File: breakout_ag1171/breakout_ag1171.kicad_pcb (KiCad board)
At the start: 2 copper layers, 70 x 60 mm, 28 parts, among them J1 EXT1, J2 EXT2, J3 Barrel_Jack_Switch, J4 6P6C, J5 FTDI, Q1 Q_NPN_BCE, U1 Ag1171

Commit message: Add KiBot and pdf outputs for breakout_ag1171
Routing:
- net /RING: track 67.7 -> 60.4 mm
- net /TIP: track 69.0 -> 67.0 mm
- net +3V3: track 141.7 -> 140.6 mm
- net GND: track 9.75 -> 10.8 mm, vias 5 -> 6
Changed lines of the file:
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@@
 	(footprint "Diode_THT:D_DO-35_SOD27_P12.70mm_Horizontal"
 		(layer "F.Cu")
-		(at 138.03 107.175)
+		(at 138.06 107.175)
 		(descr "Diode, DO-35_SOD27 series, Axial, Horizontal, pin pitch=12.7mm, , length*diameter=4*2mm^2, , http://www.diodes.com/_files/packages/DO-35.pdf")
 		(tags "Diode DO-35_SOD27 series Axial Horizontal pin pitch 12.7mm  length 4mm diameter 2mm")
@@
 	)
 	(segment
-		(start 124.925 89.941)
+		(start 120.37 98.19)
 		(end 124.925 98.19)
 		(width 0.254)
@@
 	(segment
 		(start 113.03 87.73)
-		(end 122.714 87.73)
-		(width 0.254)
-		(layer "F.Cu")
-		(net 3)
-	)
-	(segment
-		(start 120.37 98.19)
-		(end 124.925 98.19)
+		(end 126.79 87.73)
 		(width 0.254)
 		(layer "F.Cu")
@@
 	)
 	(segment
-		(start 122.714 87.73)
-		(end 124.925 89.941)
-		(width 0.254)
-		(layer "F.Cu")
-		(net 3)
-	)
-	(segment
 		(start 127.1475 98.19)
 		(end 120.37 98.19)
@@
 	)
 	(segment
-		(start 118.956 103.53)
-		(end 118.956 107.213)
+		(start 112.43 100.93)
+		(end 112.43 107.63)
 		(width 0.254)
 		(layer "F.Cu")
@@
 	)
 	(segment
-		(start 128.9525 96.5475)
-		(end 129.33 96.17)
-		(width 0.254)
-		(layer "F.Cu")
-		(net 4)
-	)
-	(segment
-		(start 118.956 107.213)
-		(end 120.188 108.445)
-		(width 0.254)
-		(layer "F.Cu")
-		(net 4)
-	)
-	(segment
-		(start 112.43 107.63)
-		(end 112.43 103.452)
+		(start 129.33 96.17)
+		(end 129.33 70.78)
 		(width 0.254)
 		(layer "F.Cu")
@@
 	)
 	(segment
-		(start 126.741 108.445)
-		(end 128.9525 106.2335)
+		(start 117.83 97.17)
+		(end 116.19 97.17)
 		(width 0.254)
 		(layer "F.Cu")
@@
 	)
 	(segment
-		(start 117.83 97.17)
-		(end 116.299 97.17)
+		(start 116.19 97.17)
+		(end 112.43 100.93)
 		(width 0.254)
 		(layer "F.Cu")
@@
 	)
 	(segment
-		(start 115.654 100.228)
-		(end 118.956 103.53)
+		(start 124.985 108.445)
+		(end 126.741 108.445)
 		(width 0.254)
 		(layer "F.Cu")
@@
 	)
 	(segment
-		(start 115.654 97.815)
-		(end 115.654 100.228)
+		(start 124.17 107.63)
+		(end 124.985 108.445)
 		(width 0.254)
 		(layer "F.Cu")
@@
 	)
 	(segment
-		(start 116.299 97.17)
-		(end 115.654 97.815)
+		(start 126.741 108.445)
+		(end 128.9525 106.2335)
 		(width 0.254)
 		(layer "F.Cu")
@@
 	)
 	(segment
-		(start 120.188 108.445)
-		(end 126.741 108.445)
+		(start 128.9525 96.5475)
+		(end 129.33 96.17)
 		(width 0.254)
 		(layer "F.Cu")
@@
 	)
 	(segment
-		(start 129.33 96.17)
-		(end 129.33 70.78)
+		(start 112.43 107.63)
+		(end 124.17 107.63)
 		(width 0.254)
 		(layer "F.Cu")
@@
 	)
 	(segment
-		(start 112.43 103.452)
-		(end 115.654 100.228)
+		(start 133.853 108.445)
+		(end 135.123 107.175)
 		(width 0.254)
 		(layer "F.Cu")
-		(net 4)
+		(net 5)
 	)
 	(segment
-		(start 137.992 107.213)
+		(start 135.123 107.175)
 		(end 138.03 107.175)
 		(width 0.254)
@@
 	)
 	(segment
-		(start 135.085 107.213)
-		(end 137.992 107.213)
-		(width 0.254)
-		(layer "F.Cu")
-		(net 5)
-	)
-	(segment
-		(start 133.853 108.445)
-		(end 135.085 107.213)
-		(width 0.254)
-		(layer "F.Cu")
-		(net 5)
-	)
-	(segment
 		(start 111.082 72.034)
 		(end 111.086 72.03)
@@
 	)
 	(segment
-		(start 165.68 71.57)
-		(end 164.89 70.78)
-		(width 0.508)
+		(start 113.04 83.083)
+		(end 113.04 81.905)
+		(width 0.254)
 		(layer "F.Cu")
 		(net 6)
@@
 	(segment
 		(start 165.68 74)
-		(end 165.68 71.57)
+		(end 164.592 74)
 		(width 0.508)
 		(layer "F.Cu")
@@
 	)
 	(segment
-		(start 113.04 83.083)
-		(end 113.04 81.905)
-		(width 0.254)
+		(start 165.68 74)
+		(end 165.68 71.57)
+		(width 0.508)
 		(layer "F.Cu")
 		(net 6)
@@
 	)
 	(segment
+		(start 165.68 71.57)
+		(end 164.89 70.78)
+		(width 0.508)
+		(layer "F.Cu")
+		(net 6)
+	)
+	(segment
 		(start 132.164 105.905)
 		(end 131.135 105.905)
@@
 	)
 	(via
+		(at 164.592 74)
+		(size 1)
+		(drill 0.5)
+		(layers "F.Cu" "B.Cu")
+		(net 6)
+	)
+	(via
 		(at 111.082 68.03)
 		(size 0.6)
@@
 	)
 	(segment
-		(start 167.851 78.003)
-		(end 166.64 76.792)
-		(width 0.508)
-		(layer "F.Cu")
-		(net 10)
-	)
-	(segment
-		(start 166.64 71.57)
-		(end 167.43 70.78)
+		(start 171.28 79.273)
+		(end 170.01 78.003)
 		(width 0.508)
 		(layer "F.Cu")
@@
 	)
 	(segment
-		(start 146.134 110.134)
-		(end 163.026 110.134)
+		(start 144.445 113.555)
+		(end 147 111)
 		(width 0.508)
 		(layer "F.Cu")
@@
 	)
 	(segment
-		(start 164.765 108.395)
-		(end 164.765 95.745)
-		(width 0.508)
-		(layer "F.Cu")
-		(net 10)
-	)
-	(segment
-		(start 144.445 118.605)
-		(end 144.445 111.823)
+		(start 147 111)
+		(end 162 111)
 		(width 0.508)
 		(layer "F.Cu")
@@
 	)
 	(segment
-		(start 167.43 67.676)
-		(end 167.43 70.78)
+		(start 162 111)
+		(end 164.765 108.235)
 		(width 0.508)
 		(layer "F.Cu")
@@
 	)
 	(segment
-		(start 166.64 74)
-		(end 166.64 71.57)
+		(start 164.765 108.235)
+		(end 164.765 95.745)
 		(width 0.508)
 		(layer "F.Cu")
@@
 	)
 	(segment
-		(start 166.64 76.792)
-		(end 166.64 74)
+		(start 167.43 67.676)
+		(end 167.43 70.78)
 		(width 0.508)
 		(layer "F.Cu")
@@
 	)
 	(segment
-		(start 171.28 86.766)
-		(end 171.28 84.607)
+		(start 166.64 76.792)
+		(end 166.64 73)
 		(width 0.508)
 		(layer "F.Cu")
@@
 	)
 	(segment
-		(start 144.445 111.823)
-		(end 146.134 110.134)
+		(start 171.28 86.766)
+		(end 171.28 84.607)
 		(width 0.508)
 		(layer "F.Cu")
@@
 	)
 	(segment
-		(start 170.01 78.003)
-		(end 167.851 78.003)
+		(start 166.64 73)
+		(end 166.64 71.57)
 		(width 0.508)
 		(layer "F.Cu")
@@
 	)
 	(segment
+		(start 144.445 118.605)
+		(end 144.445 113.555)
+		(width 0.508)
+		(layer "F.Cu")
+		(net 10)
+	)
+	(segment
 		(start 122.707 76.03)
 		(end 120.9425 76.03)
@@
 	)
 	(segment
-		(start 171.28 79.273)
-		(end 170.01 78.003)
+		(start 170.01 78.003)
+		(end 167.851 78.003)
 		(width 0.508)
 		(layer "F.Cu")
@@
 	)
 	(segment
-		(start 163.026 110.134)
-		(end 164.765 108.395)
+		(start 124.914 65.784)
+		(end 165.538 65.784)
 		(width 0.508)
 		(layer "F.Cu")
@@
 	)
 	(segment
-		(start 124.914 65.784)
-		(end 165.538 65.784)
+		(start 167.851 78.003)
+		(end 166.64 76.792)
 		(width 0.508)
 		(layer "F.Cu")
@@
 		(width 0.508)
 		(layer "F.Cu")
+		(net 10)
+	)
+	(segment
+		(start 166.64 71.57)
+		(end 167.43 70.78)
+		(width 0.508)
+		(layer "F.Cu")

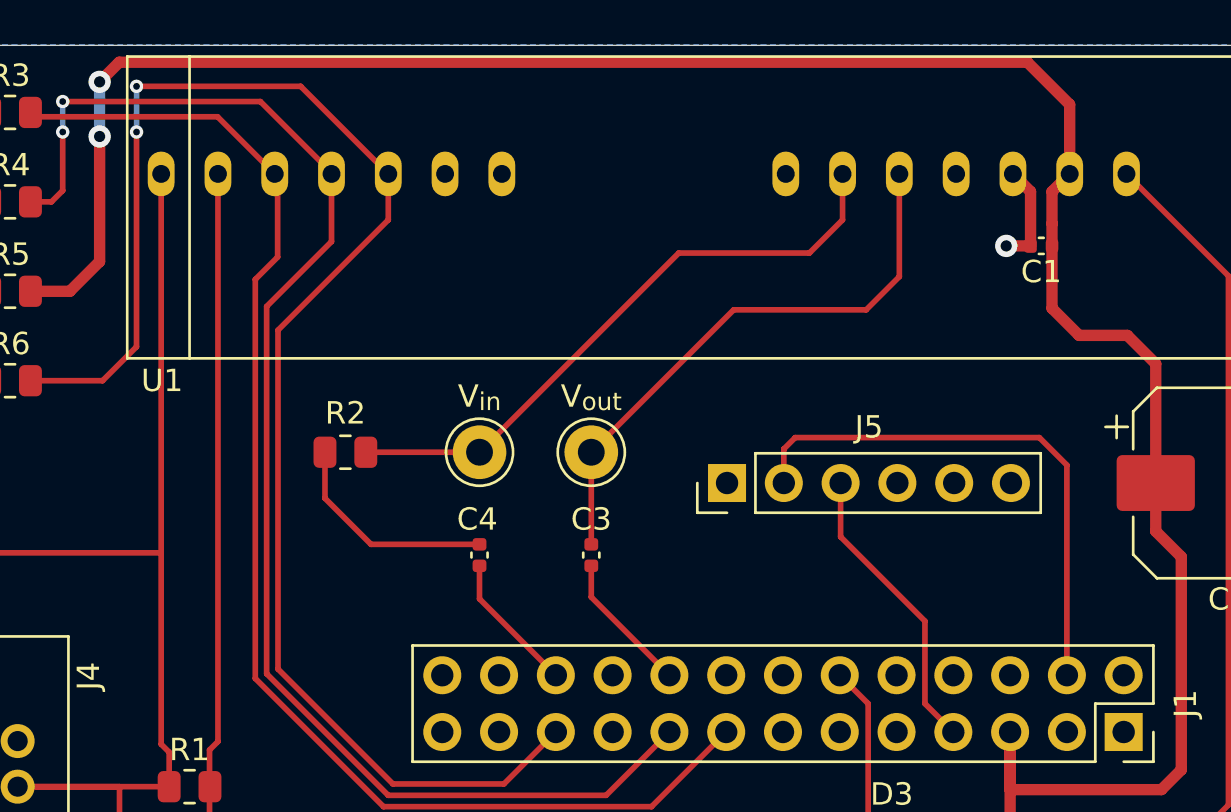
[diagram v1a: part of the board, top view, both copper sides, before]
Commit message: Fix wrong audio channel connections
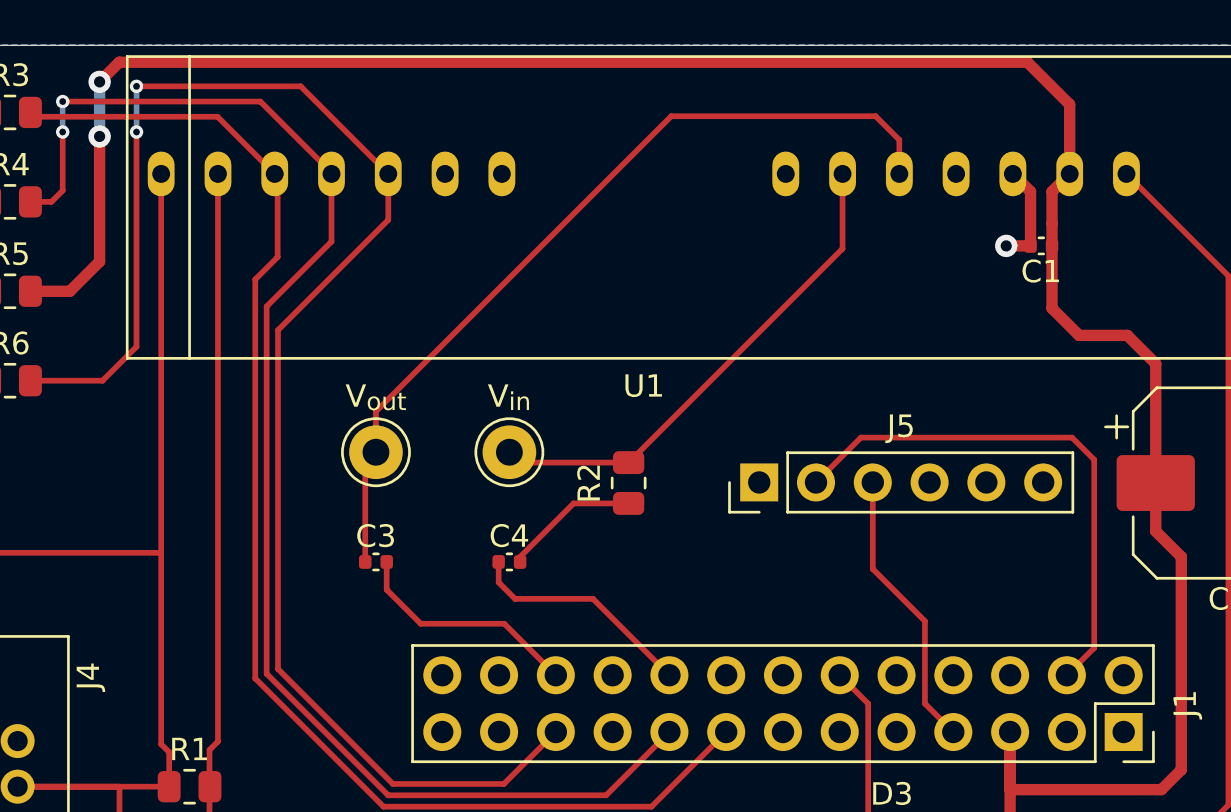
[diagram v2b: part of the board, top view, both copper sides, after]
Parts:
- moved R2 12.7 mm to (147.7, 84.6), turned to 90 degrees
- moved C3 9.64 mm to (136.4, 88.1), turned to 180 degrees
- moved TP3 9.63 mm to (136.4, 83.2)
- moved J5 1.44 mm to (153.5, 84.6)
- moved C4 1.37 mm to (142.4, 88.1), turned to 0 degrees
- moved TP4 1.34 mm to (142.4, 83.2)
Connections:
- C3 pad 1: /DAC -> /ADC
- C4 pad 1: /ADC -> /DAC
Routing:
- net Net-(U1-V_{out}): track 25.7 -> 37.8 mm
- net Net-(U1-V_{in}): track 27.7 -> 22.4 mm
- net /ADC: track 6.31 -> 10.4 mm
- net /DAC: track 6.34 -> 10.3 mm
- net Net-(C4-Pad2): track 9.83 -> 6.07 mm
- net /UART_RX: track 13.2 -> 12.7 mm

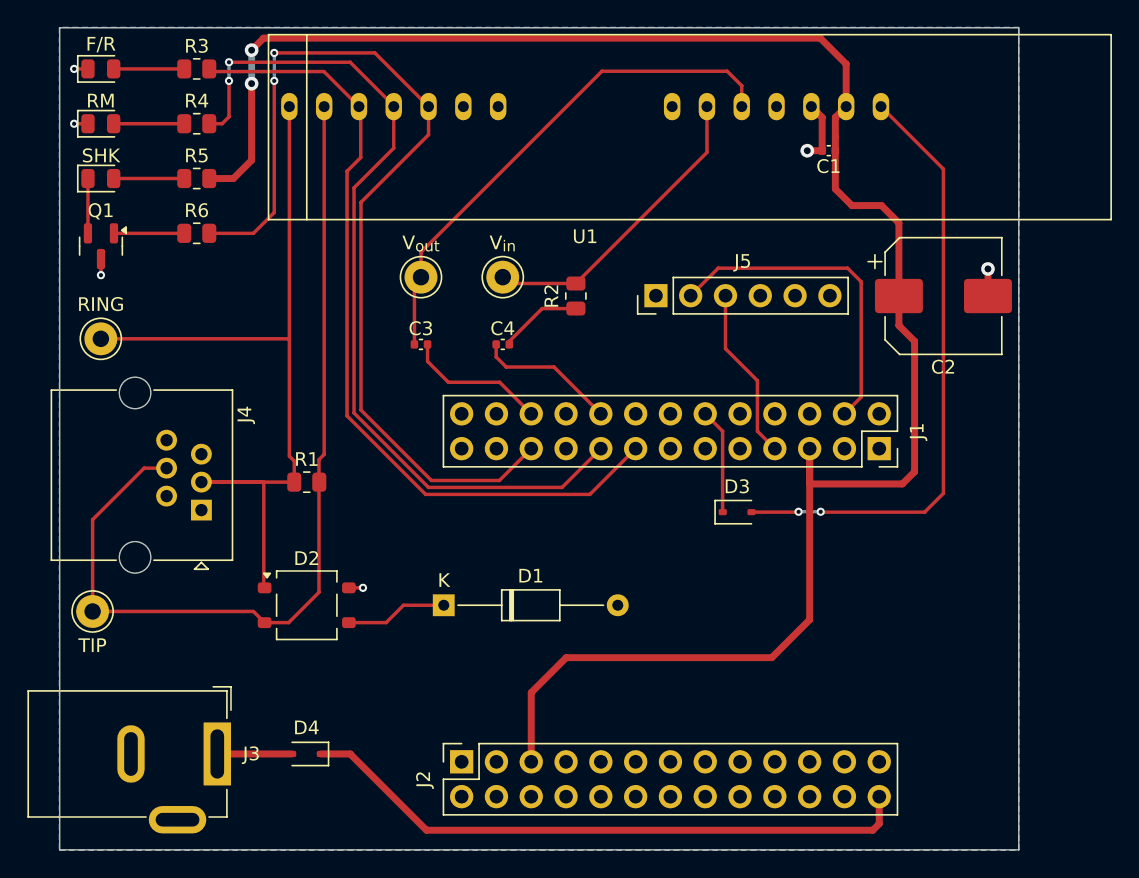
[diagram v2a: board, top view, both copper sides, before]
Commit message: Exclude U1 from BOM
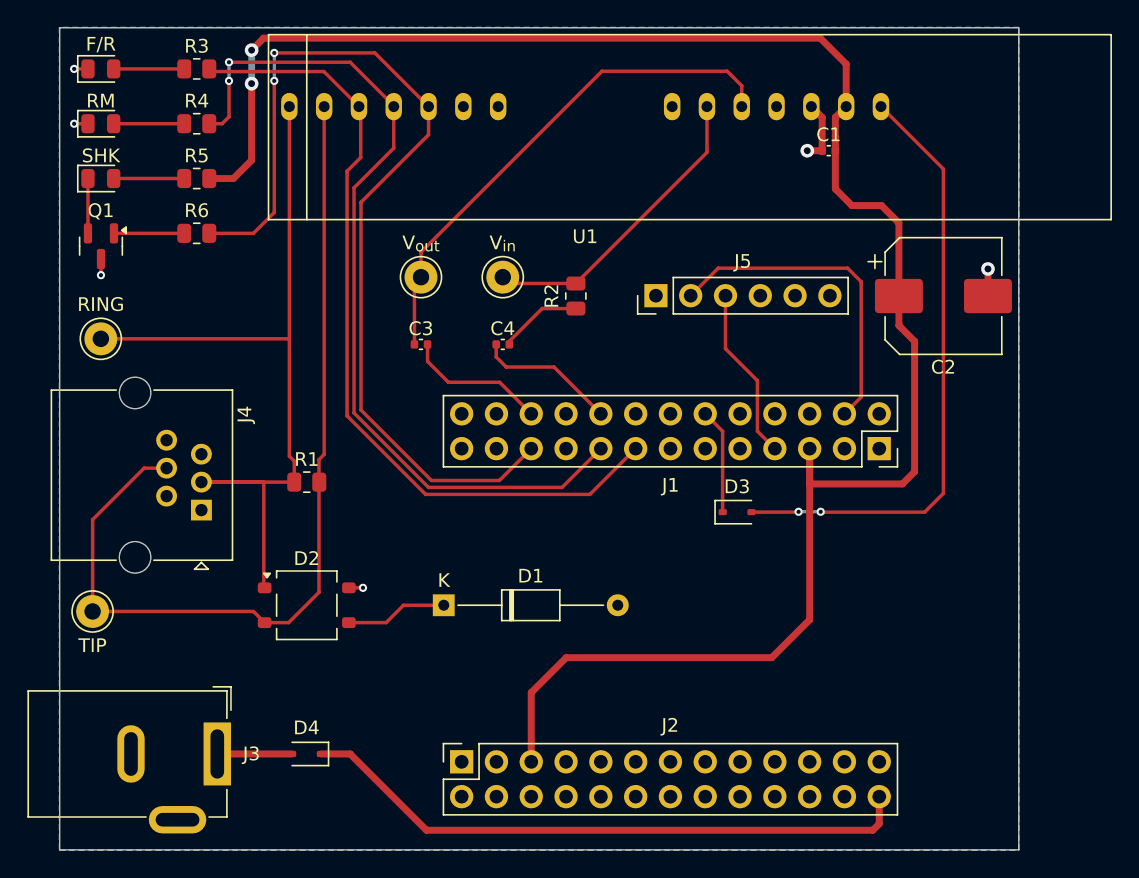
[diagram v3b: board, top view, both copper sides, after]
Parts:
- turned C1 to 0 degrees
- turned C3 to 0 degrees
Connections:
- C1 pad 1: +3V3 -> GND
- C1 pad 2: GND -> +3V3
- C3 pad 1: /ADC -> Net-(U1-V_{out})
- C3 pad 2: Net-(U1-V_{out}) -> /ADC
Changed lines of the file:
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@@
 		)
 		(property "Value" "100n"
-			(at 0 1.16 360)
+			(at 0 1.16 0)
 			(layer "F.Fab")
 			(effects
@@
 		)
 		(fp_text user "${REFERENCE}"
-			(at 0 0 360)
+			(at 0 0 0)
 			(layer "F.Fab")
 			(effects
@@
 	(footprint "Capacitor_SMD:C_0402_1005Metric"
 		(layer "F.Cu")
-		(at 166.16 74 180)
+		(at 166.16 74)
 		(descr "Capacitor SMD 0402 (1005 Metric), square (rectangular) end terminal, IPC_7351 nominal, (Body size source: IPC-SM-782 page 76, https://www.pcb-3d.com/wordpress/wp-content/uploads/ipc-sm-782a_amendment_1_and_2.pdf), generated with kicad-footprint-generator")
 		(tags "capacitor")
@@
 		)
 		(property "Footprint" "Capacitor_SMD:C_0402_1005Metric"
-			(at 0 0 180)
+			(at 0 0 0)
 			(unlocked yes)
 			(layer "F.Fab")
@@
 		)
 		(property "Datasheet" ""
-			(at 0 0 180)
+			(at 0 0 0)
 			(unlocked yes)
 			(layer "F.Fab")
@@
 		)
 		(property "Description" "Unpolarized capacitor, small symbol"
-			(at 0 0 180)
+			(at 0 0 0)
 			(unlocked yes)
 			(layer "F.Fab")
@@
 		)
 		(property "LCSC" "C76991"
-			(at 0 0 180)
+			(at 0 0 0)
 			(unlocked yes)
 			(layer "F.Fab")
@@
 		(attr smd)
 		(fp_line
-			(start -0.107836 0.36)
-			(end 0.107836 0.36)
+			(start -0.107836 -0.36)
+			(end 0.107836 -0.36)
 			(stroke
 				(width 0.12)
@@
 		)
 		(fp_line
-			(start -0.107836 -0.36)
-			(end 0.107836 -0.36)
+			(start -0.107836 0.36)
+			(end 0.107836 0.36)
 			(stroke
 				(width 0.12)
@@
 		)
 		(fp_line
-			(start 0.91 0.46)
-			(end -0.91 0.46)
+			(start -0.91 -0.46)
+			(end 0.91 -0.46)
 			(stroke
 				(width 0.05)
@@
 		)
 		(fp_line
-			(start 0.91 -0.46)
-			(end 0.91 0.46)
+			(start -0.91 0.46)
+			(end -0.91 -0.46)
 			(stroke
 				(width 0.05)
@@
 		)
 		(fp_line
-			(start -0.91 0.46)
-			(end -0.91 -0.46)
+			(start 0.91 -0.46)
+			(end 0.91 0.46)
 			(stroke
 				(width 0.05)
@@
 		)
 		(fp_line
-			(start -0.91 -0.46)
-			(end 0.91 -0.46)
+			(start 0.91 0.46)
+			(end -0.91 0.46)
 			(stroke
 				(width 0.05)
@@
 		)
 		(fp_line
-			(start 0.5 0.25)
-			(end -0.5 0.25)
+			(start -0.5 -0.25)
+			(end 0.5 -0.25)
 			(stroke
 				(width 0.1)
@@
 		)
 		(fp_line
-			(start 0.5 -0.25)
-			(end 0.5 0.25)
+			(start -0.5 0.25)
+			(end -0.5 -0.25)
 			(stroke
 				(width 0.1)
@@
 		)
 		(fp_line
-			(start -0.5 0.25)
-			(end -0.5 -0.25)
+			(start 0.5 -0.25)
+			(end 0.5 0.25)
 			(stroke
 				(width 0.1)
@@
 		)
 		(fp_line
-			(start -0.5 -0.25)
-			(end 0.5 -0.25)
+			(start 0.5 0.25)
+			(end -0.5 0.25)
 			(stroke
 				(width 0.1)
@@
 		)
 		(pad "1" smd roundrect
-			(at -0.48 0 180)
+			(at -0.48 0)
 			(size 0.56 0.62)
 			(layers "F.Cu" "F.Paste" "F.Mask")
 			(roundrect_rratio 0.25)
-			(net 10 "+3V3")
+			(net 6 "GND")
 			(pintype "passive")
 		)
 		(pad "2" smd roundrect
-			(at 0.48 0 180)
+			(at 0.48 0)
 			(size 0.56 0.62)
 			(layers "F.Cu" "F.Paste" "F.Mask")
 			(roundrect_rratio 0.25)
-			(net 6 "GND")
+			(net 10 "+3V3")
 			(pintype "passive")
 		)
@@
 		(tags "Through hole socket strip THT 2x13 2.54mm double row")
 		(property "Reference" "J1"
-			(at -1.27 -2.77 90)
+			(at 2.68 15.225 180)
 			(layer "F.SilkS")
 			(effects
@@
 		(sheetname "Root")
 		(sheetfile "breakout_ag1171.kicad_sch")
-		(attr through_hole)
+		(attr through_hole exclude_from_bom)
 		(fp_line
 			(start -23.11 -5.25)
@@
 		(tags "Through hole socket strip THT 2x13 2.54mm double row")
 		(property "Reference" "J2"
-			(at -1.27 -2.77 90)
+			(at 2.654 15.225 180)
 			(layer "F.SilkS")
 			(effects
@@
 	(footprint "Capacitor_SMD:C_0402_1005Metric"
 		(layer "F.Cu")
-		(at 136.398 88.138 180)
+		(at 136.398 88.138)
 		(descr "Capacitor SMD 0402 (1005 Metric), square (rectangular) end terminal, IPC_7351 nominal, (Body size source: IPC-SM-782 page 76, https://www.pcb-3d.com/wordpress/wp-content/uploads/ipc-sm-782a_amendment_1_and_2.pdf), generated with kicad-footprint-generator")
 		(tags "capacitor")
 		(property "Reference" "C3"
-			(at 0 1.143 180)
+			(at 0 -1.143 0)
 			(layer "F.SilkS")
 			(effects
@@
 		)
 		(property "Value" "100n"
-			(at 0 1.16 360)
+			(at 0 1.16 0)
 			(layer "F.Fab")
 			(effects
@@
 		)
 		(property "Footprint" "Capacitor_SMD:C_0402_1005Metric"
-			(at 0 0 180)
+			(at 0 0 0)
 			(unlocked yes)
 			(layer "F.Fab")
@@
 		)
 		(property "Datasheet" ""
-			(at 0 0 180)
+			(at 0 0 0)
 			(unlocked yes)
 			(layer "F.Fab")
@@
 		)
 		(property "Description" "Unpolarized capacitor, small symbol"
-			(at 0 0 180)
+			(at 0 0 0)
 			(unlocked yes)
 			(layer "F.Fab")
@@
 		)
 		(property "LCSC" "C71629"
-			(at 0 0 180)
+			(at 0 0 0)
 			(unlocked yes)
 			(layer "F.Fab")
@@
 		(attr smd)
 		(fp_line
-			(start -0.107836 0.36)
-			(end 0.107836 0.36)
+			(start -0.107836 -0.36)
+			(end 0.107836 -0.36)
 			(stroke
 				(width 0.12)
@@
 		)
 		(fp_line
-			(start -0.107836 -0.36)
-			(end 0.107836 -0.36)
+			(start -0.107836 0.36)
+			(end 0.107836 0.36)
 			(stroke
 				(width 0.12)
@@
 		)
 		(fp_line
-			(start 0.91 0.46)
-			(end -0.91 0.46)
+			(start -0.91 -0.46)
+			(end 0.91 -0.46)
 			(stroke
 				(width 0.05)
@@
 		)
 		(fp_line
-			(start 0.91 -0.46)
-			(end 0.91 0.46)
+			(start -0.91 0.46)
+			(end -0.91 -0.46)
 			(stroke
 				(width 0.05)
@@
 		)
 		(fp_line
-			(start -0.91 0.46)
-			(end -0.91 -0.46)
+			(start 0.91 -0.46)
+			(end 0.91 0.46)
 			(stroke
 				(width 0.05)
@@
 		)
 		(fp_line
-			(start -0.91 -0.46)
-			(end 0.91 -0.46)
+			(start 0.91 0.46)
+			(end -0.91 0.46)
 			(stroke
 				(width 0.05)
@@
 		)
 		(fp_line
-			(start 0.5 0.25)
-			(end -0.5 0.25)
+			(start -0.5 -0.25)
+			(end 0.5 -0.25)
 			(stroke
 				(width 0.1)
@@
 		)
 		(fp_line
-			(start 0.5 -0.25)
-			(end 0.5 0.25)
+			(start -0.5 0.25)
+			(end -0.5 -0.25)
 			(stroke
 				(width 0.1)
@@
 		)
 		(fp_line
-			(start -0.5 0.25)
-			(end -0.5 -0.25)
+			(start 0.5 -0.25)
+			(end 0.5 0.25)
 			(stroke
 				(width 0.1)
@@
 		)
 		(fp_line
-			(start -0.5 -0.25)
-			(end 0.5 -0.25)
+			(start 0.5 0.25)
+			(end -0.5 0.25)
 			(stroke
 				(width 0.1)
@@
 		)
 		(pad "1" smd roundrect
-			(at -0.48 0 180)
+			(at -0.48 0)
 			(size 0.56 0.62)
 			(layers "F.Cu" "F.Paste" "F.Mask")
 			(roundrect_rratio 0.25)
-			(net 7 "/ADC")
+			(net 61 "Net-(U1-V_{out})")
 			(pintype "passive")
 		)
 		(pad "2" smd roundrect
-			(at 0.48 0 180)
+			(at 0.48 0)
 			(size 0.56 0.62)
 			(layers "F.Cu" "F.Paste" "F.Mask")
 			(roundrect_rratio 0.25)
-			(net 61 "Net-(U1-V_{out})")
+			(net 7 "/ADC")
 			(pintype "passive")
 		)
@@
 	)
 	(segment
-		(start 144.445 93.205)
-		(end 142.1425 90.9025)
+		(start 136.878 89.38)
+		(end 136.878 88.138)
 		(width 0.254)
 		(layer "F.Cu")
@@
 	)
 	(segment
-		(start 136.878 89.38)
-		(end 136.878 88.138)
+		(start 138.4005 90.9025)
+		(end 136.878 89.38)
 		(width 0.254)
 		(layer "F.Cu")
@@
 	)
 	(segment
-		(start 138.4005 90.9025)
-		(end 136.878 89.38)
+		(start 144.445 93.205)
+		(end 142.1425 90.9025)
 		(width 0.254)
 		(layer "F.Cu")
@@
 	)
 	(segment
-		(start 135.918 83.71)
-		(end 136.398 83.23)
-		(width 0.254)
-		(layer "F.Cu")
-		(net 61)
-	)
-	(segment
 		(start 136.398 81.407)
 		(end 149.606 68.199)
@@
 	)
 	(segment
-		(start 135.918 88.138)
-		(end 135.918 83.71)
+		(start 135.918 83.71)
+		(end 136.398 83.23)
 		(width 0.254)
 		(layer "F.Cu")
@@
 		(width 0.254)
 		(layer "F.Cu")
+		(net 61)
+	)
+	(segment
+		(start 135.918 88.138)
+		(end 135.918 83.71)
+		(width 0.254)
+		(layer "F.Cu")
